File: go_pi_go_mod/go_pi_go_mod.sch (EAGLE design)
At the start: 18 parts, among them J1 HC_SR04, M1 LEFT_MOTOR, M2 RIGHT_MOTOR, M3 SERVO, Q1 PN2222A, Q2 PN2222A

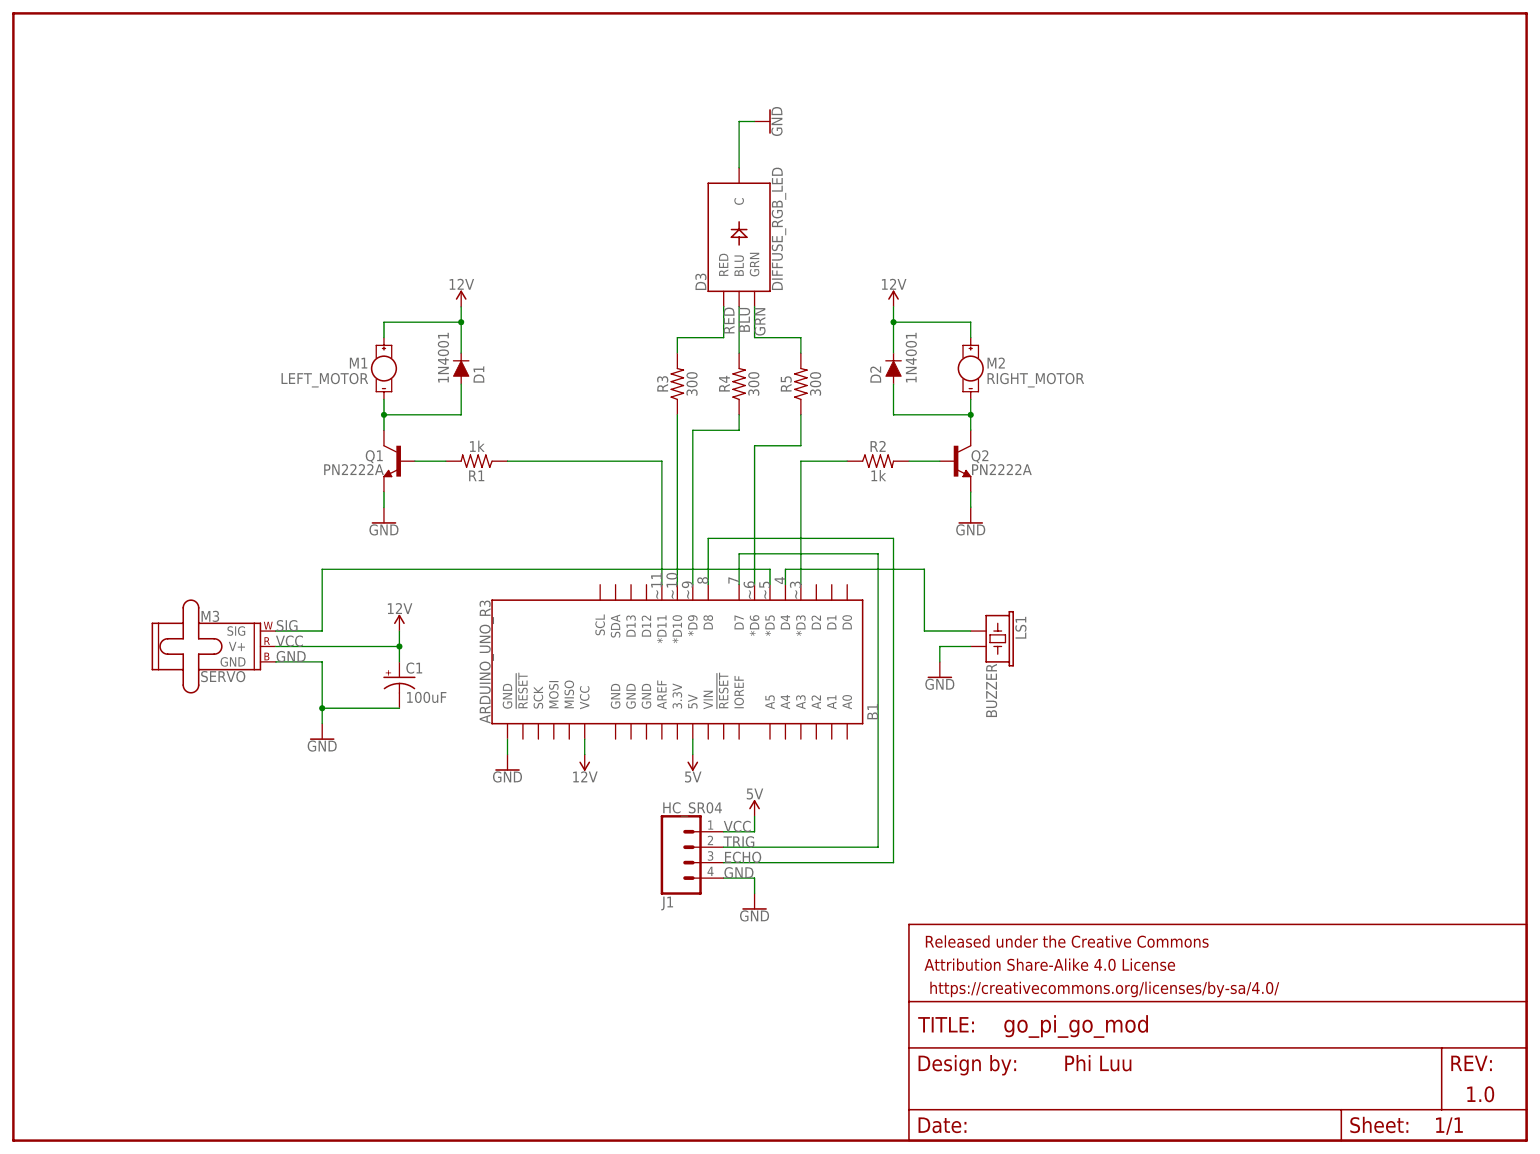
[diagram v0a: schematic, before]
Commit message: Make change to the GoPiGo Mod schematic (simplification)
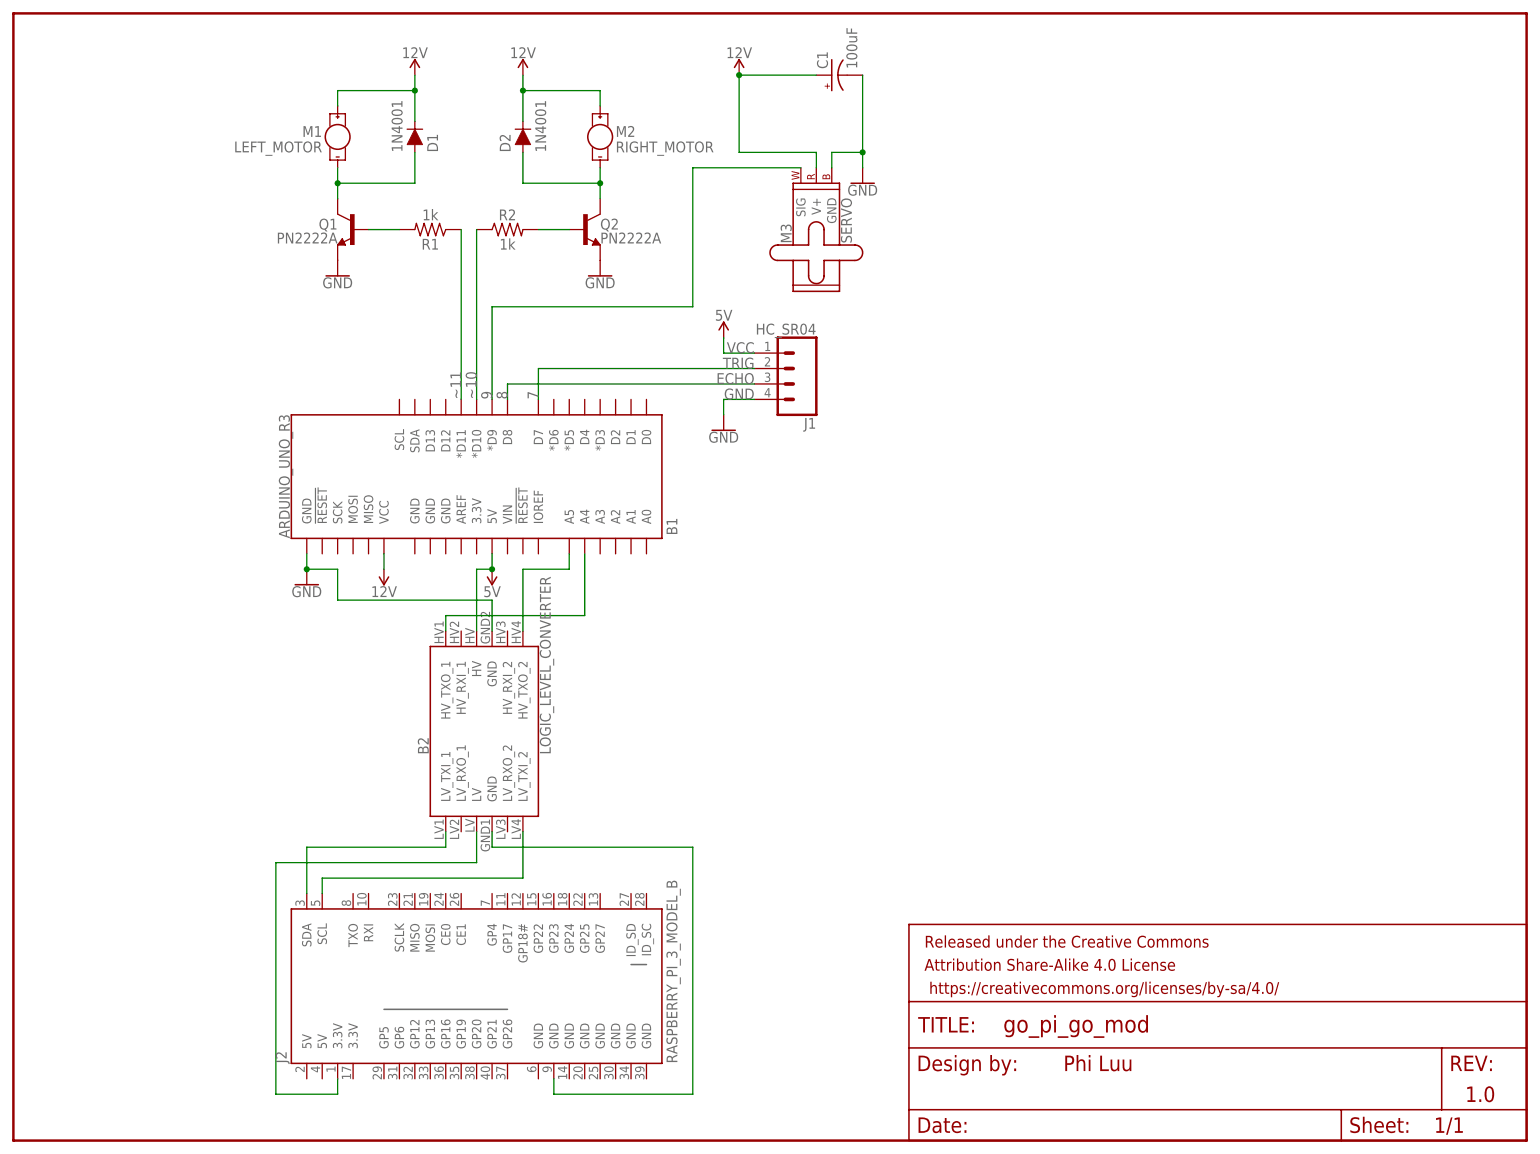
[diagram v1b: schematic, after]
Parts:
- removed D3: DIFFUSE_RGB_LED, SparkFun-LED:LED-RGB-CCDIFFUSE
- removed LS1: BUZZER, SparkFun-Electromechanical:BUZZER-PTH
- removed R3, R4, R5: 300, SparkFun-Resistors:1KOHM-HORIZ-1/4W-5%
- added B2: LOGIC_LEVEL_CONVERTER, SparkFun-Boards:SPARKFUN_LOGIC_LEVEL_CONVERTER
- added J2: RASPBERRY_PI_3_MODEL_B, SparkFun-Connectors:RASPBERRYPI-40-PIN-GPIO_PTH
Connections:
- removed net 4: B1.D4, LS1.1
- removed net BLU: D3.BLU, R4.2
- removed net GRN: D3.GRN, R5.2
- removed net RED: D3.RED, R3.2
- removed net ~3: B1.*D3, R2.1
- removed net ~5: B1.*D5, M3.SIG
- removed net ~6: B1.*D6, R5.1
- removed net ~9: B1.*D9, R4.1
- new net 3.3V: B2.LV, J2.3.3V@1
- new net 9: B1.*D9, M3.SIG
- new net A4: B1.A4, B2.HV_TXO_1
- new net A5: B1.A5, B2.HV_TXO_2
- new net SCL: B2.LV_TXI_2, J2.SCL
- new net SDA: B2.LV_TXI_1, J2.SDA
- net 5V: now also B2.HV
- net GND: now also B2.GND, B2.GND@2, J2.GND@9; no longer D3.C, LS1.2
- net ~10: now also R2.1; no longer R3.1
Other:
- note removed: "SIG"
- moved on the sheet: B1, C1, D1, D2, J1, M1, M2, M3, Q1, Q2, R1, R2
